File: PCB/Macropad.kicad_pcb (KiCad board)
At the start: 2 copper layers, 65 x 55.5 mm, 8 parts, among them J1 Conn_01x04_MountingPin, SW1 SW_Push, SW10 RotaryEncoder_Switch, SW2 SW_Push, SW4 SW_Push, SW5 SW_Push, SW6 SW_Push, U1 MOUDLE-SEEEDUINO-XIAO

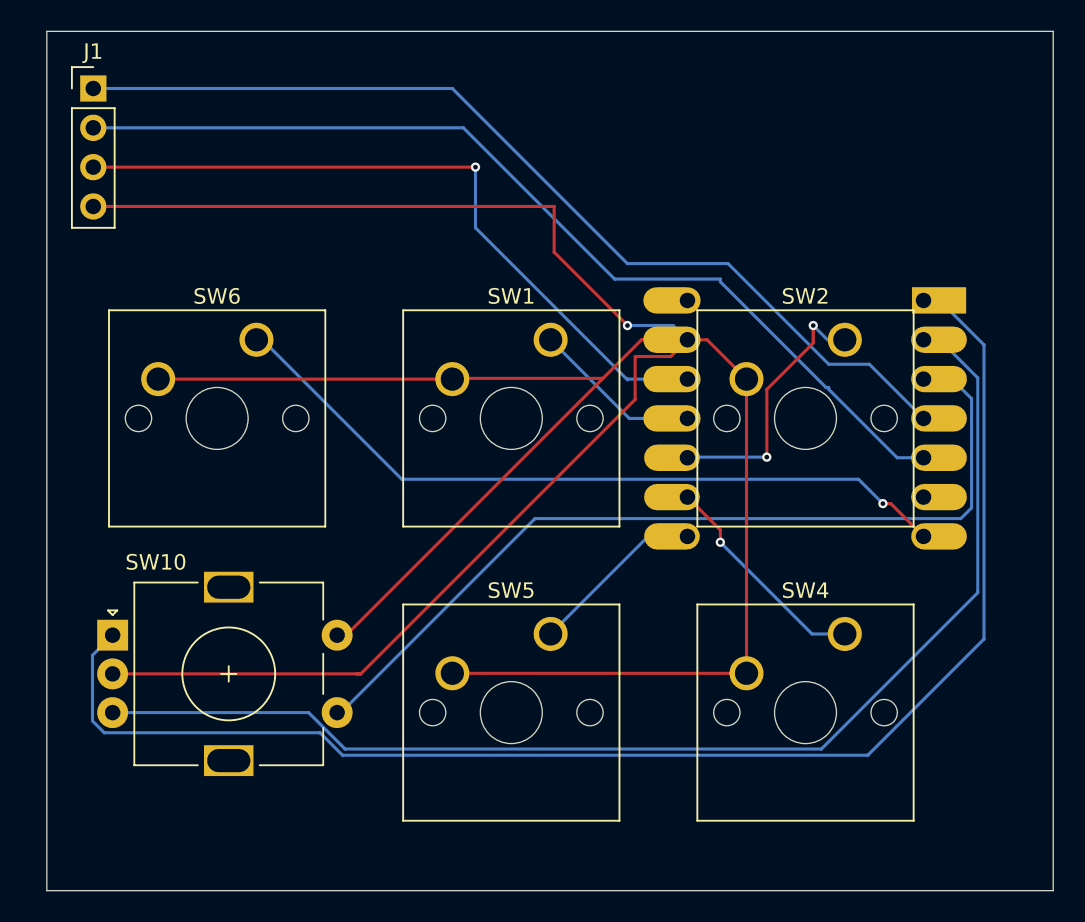
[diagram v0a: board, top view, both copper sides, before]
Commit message: Case design update, PCB tweaks
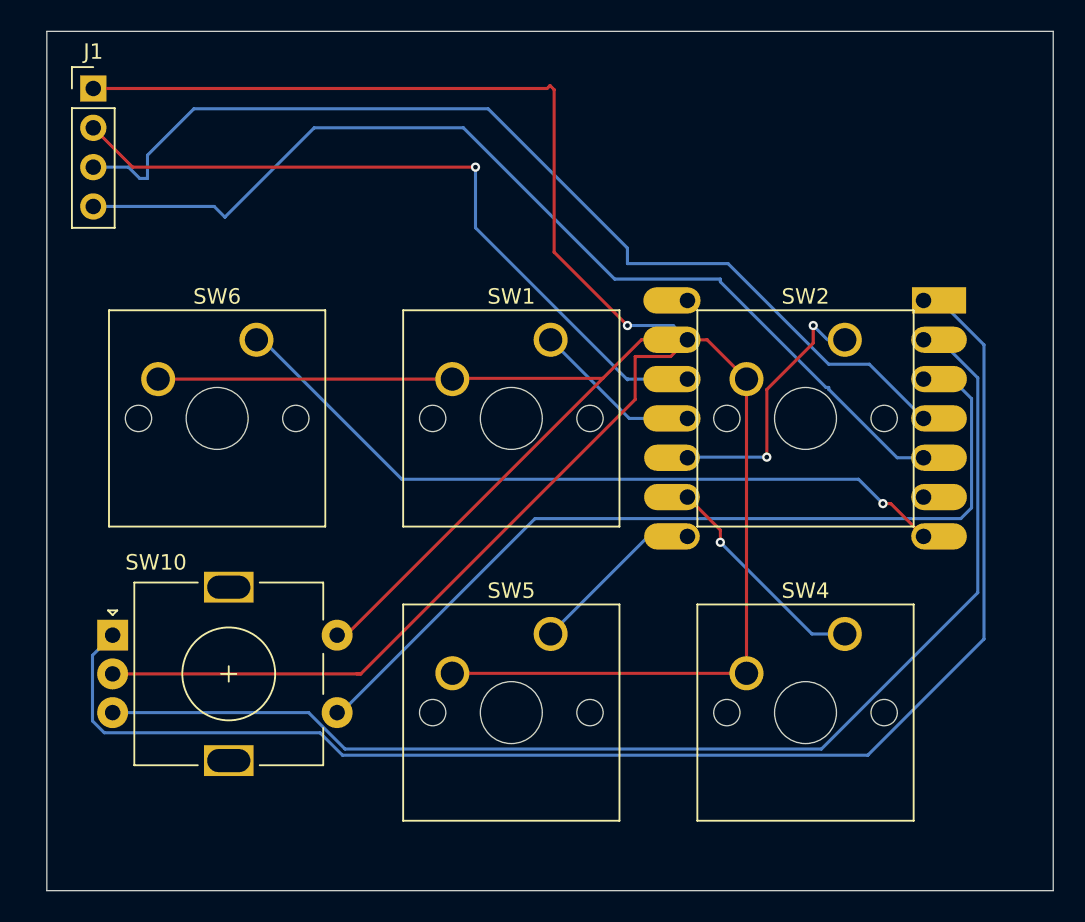
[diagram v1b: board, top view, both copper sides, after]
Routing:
- net GND: track 365.7 -> 380.3 mm
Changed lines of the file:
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@@
-	)
-	(segment
-		(start 95 49.31)
-		(end 124.765 49.31)
-		(width 0.2)
-		(layer "F.Cu")
-		(net 2)
 	)
 	(segment
@@
 	)
 	(segment
+		(start 129.5 57)
+		(end 124.765 52.265)
+		(width 0.2)
+		(layer "F.Cu")
+		(net 2)
+	)
+	(segment
 		(start 118.237592 60.412408)
 		(end 127.912408 60.412408)
@@
 	)
 	(segment
-		(start 124.765 52.265)
-		(end 129.5 57)
-		(width 0.2)
-		(layer "F.Cu")
-		(net 2)
-	)
-	(segment
-		(start 124.765 49.31)
-		(end 124.765 52.265)
-		(width 0.2)
-		(layer "F.Cu")
-		(net 2)
-	)
-	(segment
 		(start 110.75 77)
 		(end 111.324816 77)
@@
 	)
 	(segment
+		(start 124.5 41.5)
+		(end 124.31 41.69)
+		(width 0.2)
+		(layer "F.Cu")
+		(net 2)
+	)
+	(segment
 		(start 96.25 79.5)
 		(end 112.27847 79.5)
@@
 	)
 	(segment
+		(start 97.54 46.77)
+		(end 95 44.23)
+		(width 0.2)
+		(layer "F.Cu")
+		(net 2)
+	)
+	(segment
+		(start 119.685 46.77)
+		(end 97.54 46.77)
+		(width 0.2)
+		(layer "F.Cu")
+		(net 2)
+	)
+	(segment
 		(start 137.19 79.46)
 		(end 137.19 60.46)
@@
 	)
 	(segment
-		(start 95 46.77)
-		(end 119.685 46.77)
-		(width 0.2)
-		(layer "F.Cu")
-		(net 2)
-	)
-	(segment
 		(start 137.19 79.46)
 		(end 118.19 79.46)
@@
 	)
 	(segment
+		(start 124.765 41.765)
+		(end 124.5 41.5)
+		(width 0.2)
+		(layer "F.Cu")
+		(net 2)
+	)
+	(segment
 		(start 112.27847 79.5)
 		(end 112 79.5)
@@
 	)
 	(segment
+		(start 124.765 52.265)
+		(end 124.765 41.765)
+		(width 0.2)
+		(layer "F.Cu")
+		(net 2)
+	)
+	(segment
 		(start 130 59)
 		(end 132.295 59)
+		(width 0.2)
+		(layer "F.Cu")
+		(net 2)
+	)
+	(segment
+		(start 124.31 41.69)
+		(end 95 41.69)
 		(width 0.2)
 		(layer "F.Cu")
@@
 	)
 	(segment
+		(start 102.81 49.31)
+		(end 95 49.31)
+		(width 0.2)
+		(layer "B.Cu")
+		(net 2)
+	)
+	(segment
 		(start 128.675184 54)
 		(end 135.5 54)
@@
 	)
 	(segment
-		(start 145.125 59.5)
-		(end 148.625 63)
-		(width 0.2)
-		(layer "B.Cu")
-		(net 2)
-	)
-	(segment
-		(start 136 53)
-		(end 142.5 59.5)
+		(start 118.905184 44.23)
+		(end 109.27 44.23)
+		(width 0.2)
+		(layer "B.Cu")
+		(net 2)
+	)
+	(segment
+		(start 129.5 53)
+		(end 129.5 52)
+		(width 0.2)
+		(layer "B.Cu")
+		(net 2)
+	)
+	(segment
+		(start 129.5 52)
+		(end 120.5 43)
 		(width 0.2)
 		(layer "B.Cu")
@@
 	)
 	(segment
-		(start 129.5 53)
-		(end 136 53)
+		(start 98.5 47.5)
+		(end 98 47.5)
+		(width 0.2)
+		(layer "B.Cu")
+		(net 2)
+	)
+	(segment
+		(start 120.5 43)
+		(end 101.5 43)
+		(width 0.2)
+		(layer "B.Cu")
+		(net 2)
+	)
+	(segment
+		(start 98.5 46)
+		(end 98.5 47.5)
 		(width 0.2)
 		(layer "B.Cu")
@@
 	)
 	(segment
+		(start 109.27 44.23)
+		(end 103.5 50)
+		(width 0.2)
+		(layer "B.Cu")
+		(net 2)
+	)
+	(segment
+		(start 148.625 63)
+		(end 145.125 59.5)
+		(width 0.2)
+		(layer "B.Cu")
+		(net 2)
+	)
+	(segment
 		(start 129.5 57)
 		(end 132.455 57)
@@
 	)
 	(segment
-		(start 95 44.23)
-		(end 118.905184 44.23)
-		(width 0.2)
-		(layer "B.Cu")
-		(net 2)
-	)
-	(segment
 		(start 142.5 61.11847)
 		(end 146.92153 65.54)
@@
 	)
 	(segment
-		(start 95 41.69)
-		(end 118.19 41.69)
-		(width 0.2)
-		(layer "B.Cu")
-		(net 2)
-	)
-	(segment
-		(start 118.19 41.69)
+		(start 97.27 46.77)
+		(end 95 46.77)
+		(width 0.2)
+		(layer "B.Cu")
+		(net 2)
+	)
+	(segment
+		(start 103.5 50)
+		(end 102.81 49.31)
+		(width 0.2)
+		(layer "B.Cu")
+		(net 2)
+	)
+	(segment
+		(start 136 53)
 		(end 129.5 53)
+		(width 0.2)
+		(layer "B.Cu")
+		(net 2)
+	)
+	(segment
+		(start 98 47.5)
+		(end 97.27 46.77)
 		(width 0.2)
 		(layer "B.Cu")
@@
 	)
 	(segment
-		(start 142.5 59.5)
-		(end 145.125 59.5)
+		(start 101.5 43)
+		(end 98.5 46)
 		(width 0.2)
 		(layer "B.Cu")
@@
 		(width 0.2)
 		(layer "B.Cu")
+		(net 2)
+	)
+	(segment
+		(start 142.5 59.5)
+		(end 136 53)
+		(width 0.2)
+		(layer "B.Cu")
+		(net 2)
+	)
+	(segment
+		(start 145.125 59.5)
+		(end 142.5 59.5)
+		(width 0.2)
+		(layer "B.Cu")

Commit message: PCB tweaks
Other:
- board size 65 x 55.5 mm -> 63.5 x 53.5 mm
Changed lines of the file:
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@@
 		(embedded_fonts no)
 	)
-	(gr_rect
-		(start 92 38)
-		(end 157 93.5)
+	(gr_line
+		(start 154.5 93)
+		(end 91 93)
 		(stroke
 			(width 0.05)
 			(type default)
 		)
-		(fill no)
 		(layer "Edge.Cuts")
 	)
+	(gr_line
+		(start 154.5 51)
+		(end 154.5 93)
+		(stroke
+			(width 0.05)
+			(type default)
+		)
+		(layer "Edge.Cuts")
+	)
+	(gr_line
+		(start 91 39.5)
+		(end 91 93)
+		(stroke
+			(width 0.05)
+			(type default)
+		)
+		(layer "Edge.Cuts")
+	)
+	(gr_line
+		(start 131 51)
+		(end 131 39.5)
+		(stroke
+			(width 0.05)
+			(type default)
+		)
+		(layer "Edge.Cuts")
+	)
+	(gr_line
+		(start 131 51)
+		(end 154.5 51)
+		(stroke
+			(width 0.05)
+			(type default)
+		)
+		(layer "Edge.Cuts")
+	)
+	(gr_line
+		(start 131 39.5)
+		(end 91 39.5)
+		(stroke
+			(width 0.05)
+			(type default)
+		)
+		(layer "Edge.Cuts")
+	)

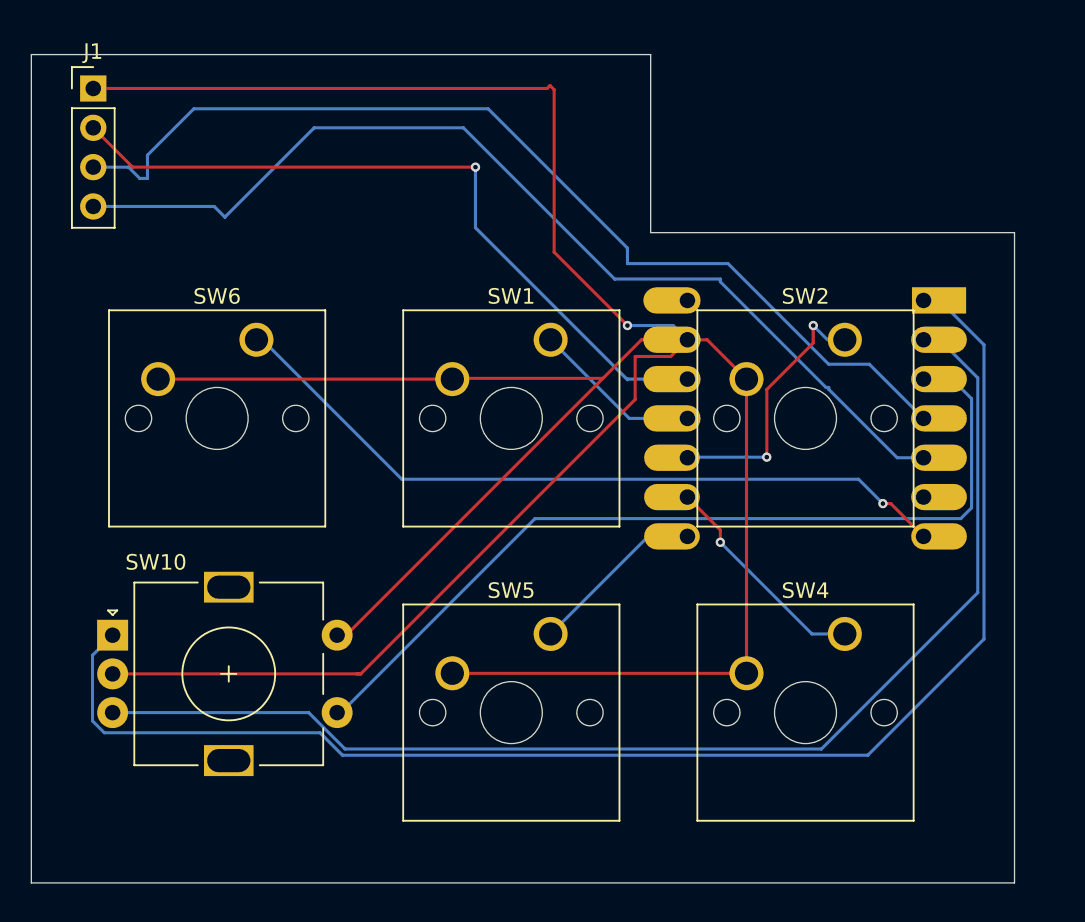
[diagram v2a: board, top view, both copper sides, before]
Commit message: Remade PCB and case
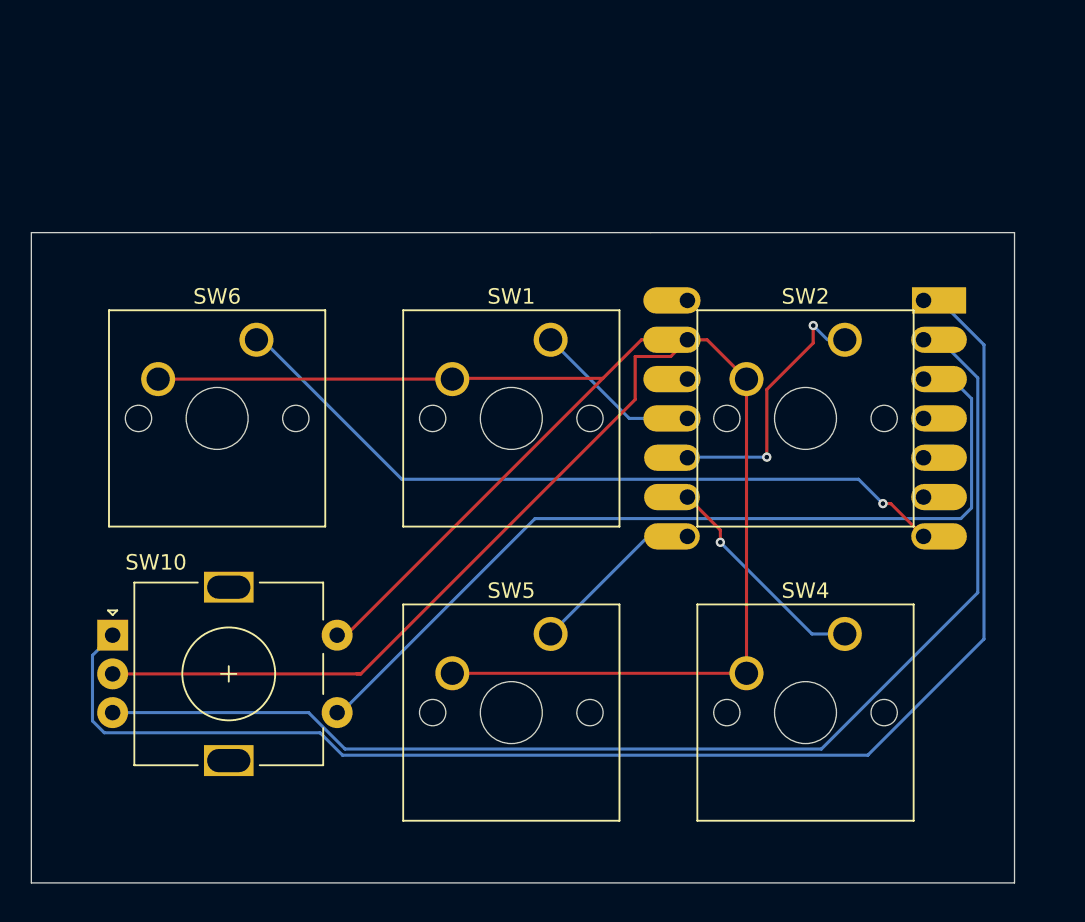
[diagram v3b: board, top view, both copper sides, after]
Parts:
- removed J1: Conn_01x04_MountingPin, Connector_PinHeader_2.54mm:PinHeader_1x04_P2.54mm_Vertical
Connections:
- SW1 pad 2: GND -> Net-(U1-3V3)
- SW2 pad 2: GND -> Net-(U1-3V3)
- SW4 pad 2: GND -> Net-(U1-3V3)
- SW5 pad 2: GND -> Net-(U1-3V3)
- SW6 pad 2: GND -> Net-(U1-3V3)
- U1 pad 12: GND -> Net-(U1-3V3)
- U1 pad 13: GND -> Net-(U1-3V3)
- U1 pad 14: GND -> Net-(U1-3V3)
- U1 pad 4: GND -> unconnected-(U1-PA11_A3_D3-Pad4)
- U1 pad 5: GND -> unconnected-(U1-PA8_A4_D4_SDA-Pad5)
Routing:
- net GND: track 380.3 -> 150.6 mm, vias 2 -> 0
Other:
- board size 63.5 x 53.5 mm -> 63.5 x 42 mm
